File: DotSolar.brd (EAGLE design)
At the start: 25 x 35 mm, 24 parts, among them IC1 CAT24M010TS, IC2 SI1145, Q1 BSH203, U1 ISL29125

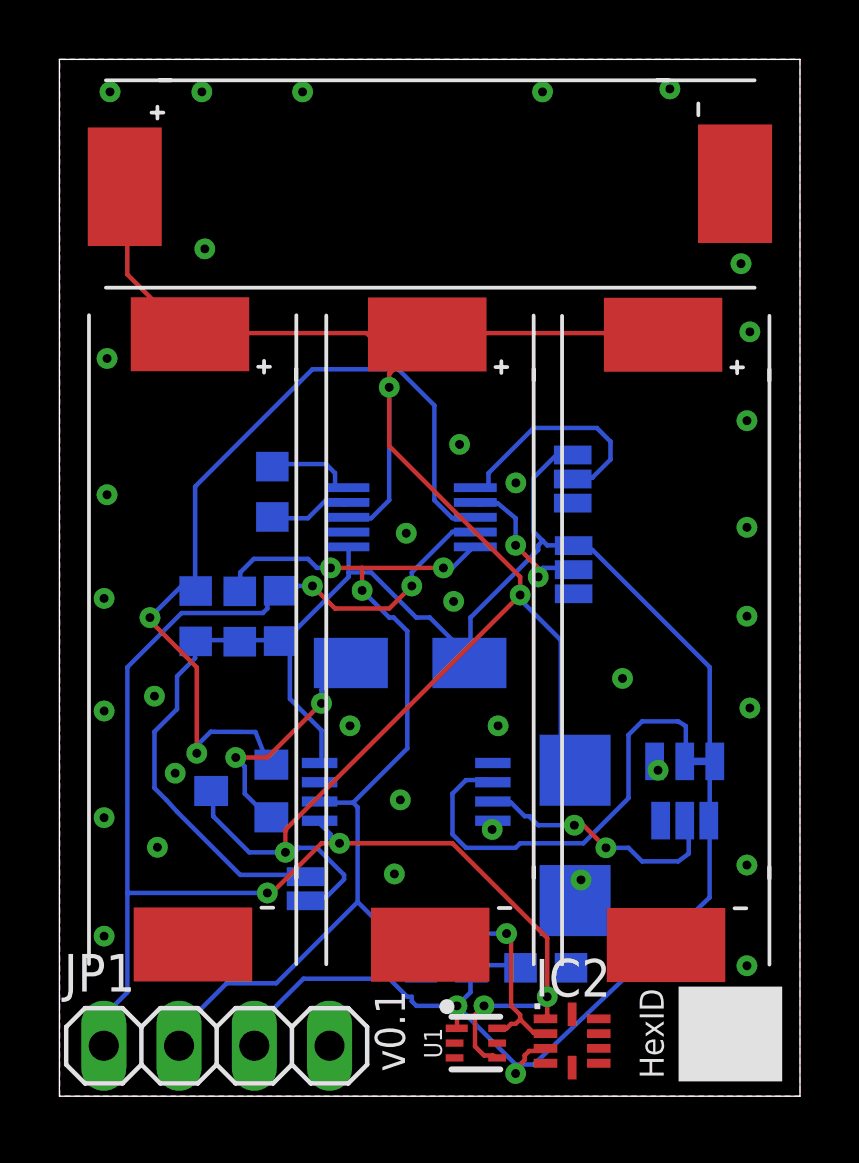
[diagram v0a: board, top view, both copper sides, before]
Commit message: Add AS3935 lightning detector
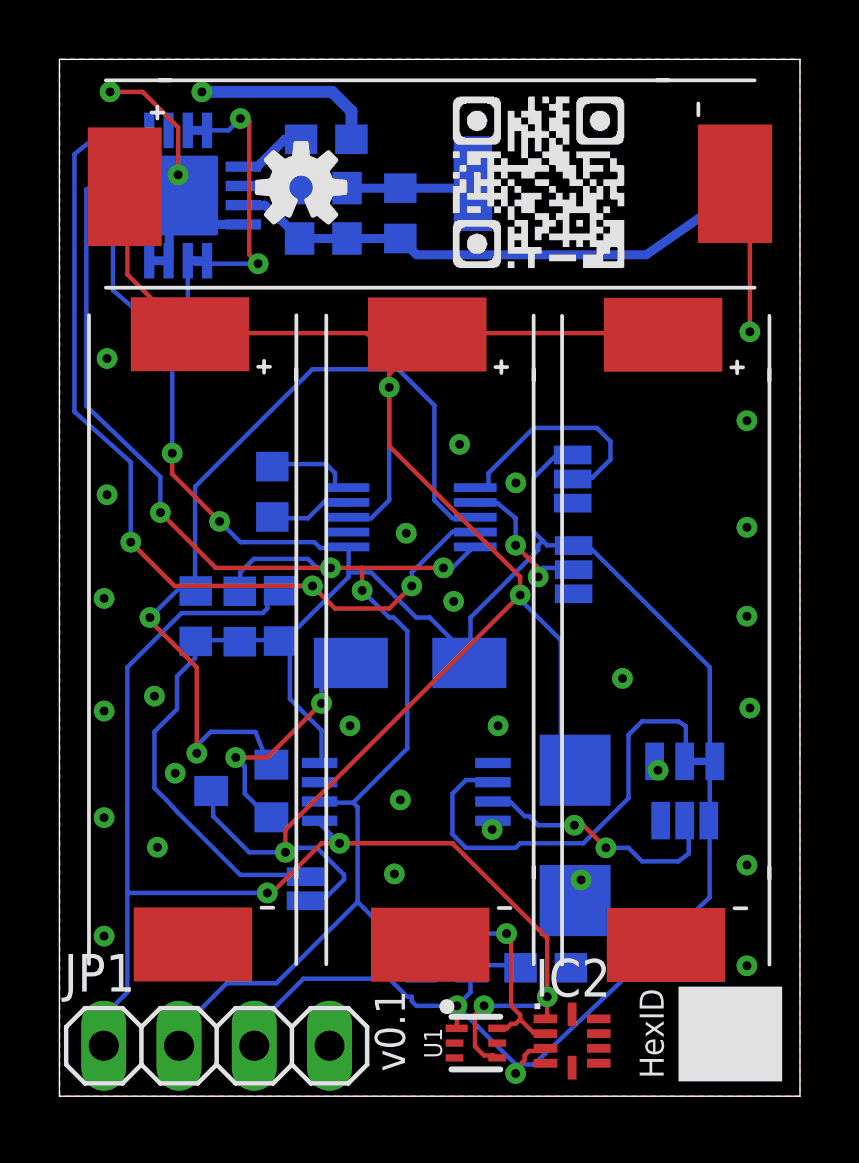
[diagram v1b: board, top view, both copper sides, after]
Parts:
- added C3: 10uF, rcl:C0603
- added C4: 680pF, rcl:C0603
- added C5: 270pF, rcl:C0603
- added IC3: (no value), AS3935:16LDMLPQ
- added R5: (no value), rcl:R0603
- added U$4: INDUCTORMA5532-AE, arducorder-mini:MA5532-AE
- moved LOGO1 14.5 mm to (8.15, 30.7), flipped to the top
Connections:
- new net INN: C4.2, C5.2, IC3.2, R5.1, U$4.2
- new net INP: C4.1, C5.1, IC3.3, R5.2, U$4.1
- new net N$3: C3.1, IC3.1
- net 3V3: now also IC3.15, IC3.16, IC3.5, IC3.6, IC3.9
- net GND: now also C3.2, IC3.12, IC3.4, IC3.7, IC3.8, IC3.EXP
- net SCL: now also IC3.11
- net SDA: now also IC3.13
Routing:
- net 3V3: track 80.0 -> 110.4 mm, vias 2 -> 6
- net GND: track 0.32 -> 26.0 mm, vias 35 -> 31
- net SDA: track 52.4 -> 75.9 mm, vias 6 -> 7
- net SCL: track 42.1 -> 61.5 mm, vias 4 -> 5
- net INP: track 0.00 -> 18.6 mm
- net INN: track 0.00 -> 7.98 mm
- net N$3: track 0.00 -> 2.33 mm
